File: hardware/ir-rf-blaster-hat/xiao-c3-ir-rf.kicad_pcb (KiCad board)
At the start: 2 copper layers, 21 x 50 mm, 18 parts, among them J1 XIAO_SOCKET_1x7, J2 XIAO_SOCKET_1x7, M1 CC1101_MODULE, Q1 SOT-23

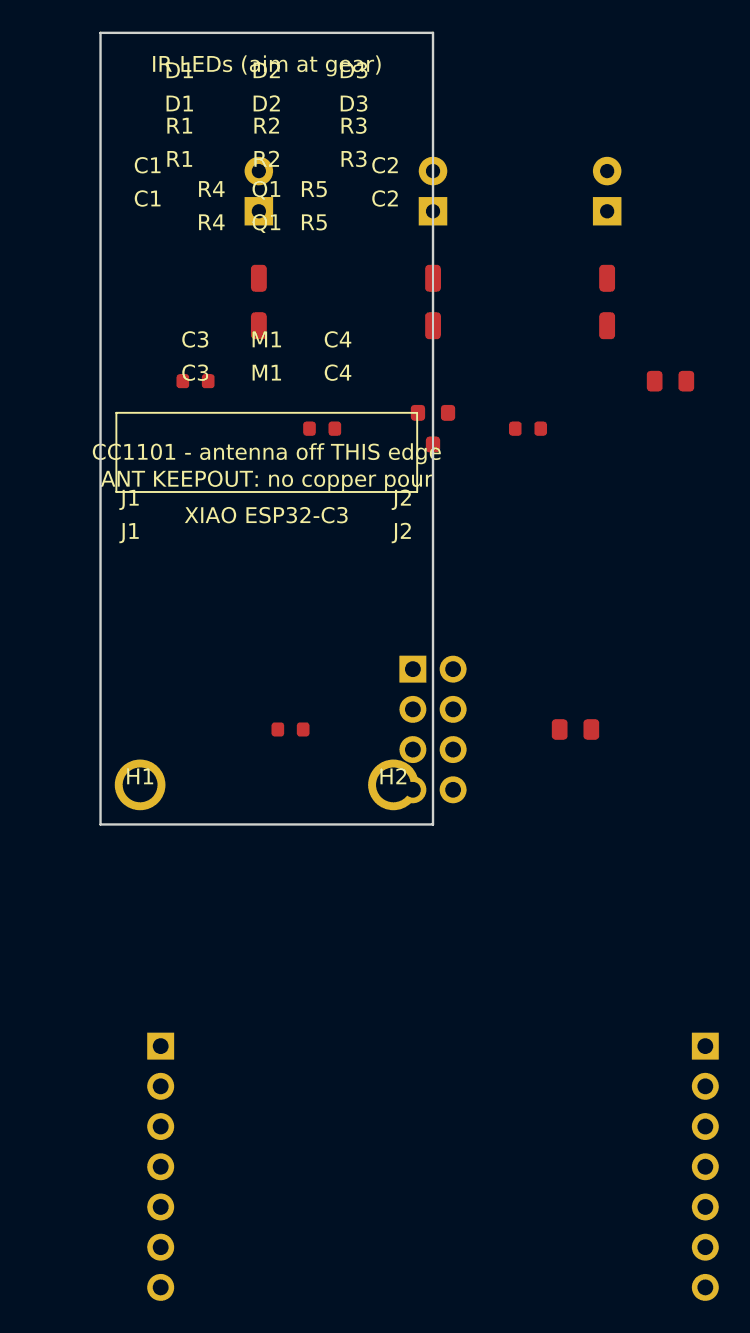
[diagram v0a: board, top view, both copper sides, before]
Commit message: feat(ir-rf-blaster): 4-layer, fully-routed, DRC-clean board (#1120)
* feat(ir-rf-blaster): 4-layer, fully-routed, DRC-clean board

Rebuild the XIAO IR+RF blaster hat as a 4-layer board, generated headlessly:
- Stackup F.Cu / In1.Cu GND plane / In2.Cu +5V plane / B.Cu. Real KiCad library
  footprints (was crude embedded geometry). GND/+5V stitched to planes via
  through-vias; +3V3 and logic signals routed on the outer layers.
- SPI fan-out uses a monotonic XIAO->CC1101 pin mapping so the traces don't cross.
- Validated with kicad-cli (KiCad 9): DRC 0 errors, 0 unconnected. Board 22x50mm.
- Ships generate_pcb.py (kiutils), fill_zones.py (pcbnew LoadBoard), the 8 footprints
  (offline-reproducible), the filled .kicad_pcb, a top render, and Gerbers/drill.

pcbnew scripting crashes under amd64 emulation on Apple Silicon (FootprintLoad), so
generation uses kiutils and zone-fill uses pcbnew.LoadBoard (which doesn't crash);
kicad-cli does DRC/export. Documented in the README.

Still GUI TODOs (flagged): swap the provisional XIAO socket for Seeed's official
footprint, and add the antenna copper keepout for the specific CC1101 module.

Co-Authored-By: Claude Opus 4.8 <noreply@anthropic.com>
Claude-Session: https://claude.ai/code/session_01NfkRErMrPyNuft1RbpzMet

* refactor(ir-rf-blaster): straighter, 45-degree, centered routing

- Straight diagonals where the line is clear (LED cathodes; SPI fan is already
  straight parallel), 45-degree chamfers on the rest (no 90-degree turns).
- Components centered east-west about the board centerline (x=11).
- Simplified the +3V3 tail to XIAO 3V3: straight drop + one 45-degree bend.
Still DRC-clean (0 errors, 0 unconnected). Re-exported Gerbers + render.

Co-Authored-By: Claude Opus 4.8 <noreply@anthropic.com>
Claude-Session: https://claude.ai/code/session_01NfkRErMrPyNuft1RbpzMet

* fix(ir-rf-blaster): center LEDs on board, fix off-board silk

Widen board to 23mm and center all components on the x=11.5 centerline so the
outer LEDs have 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
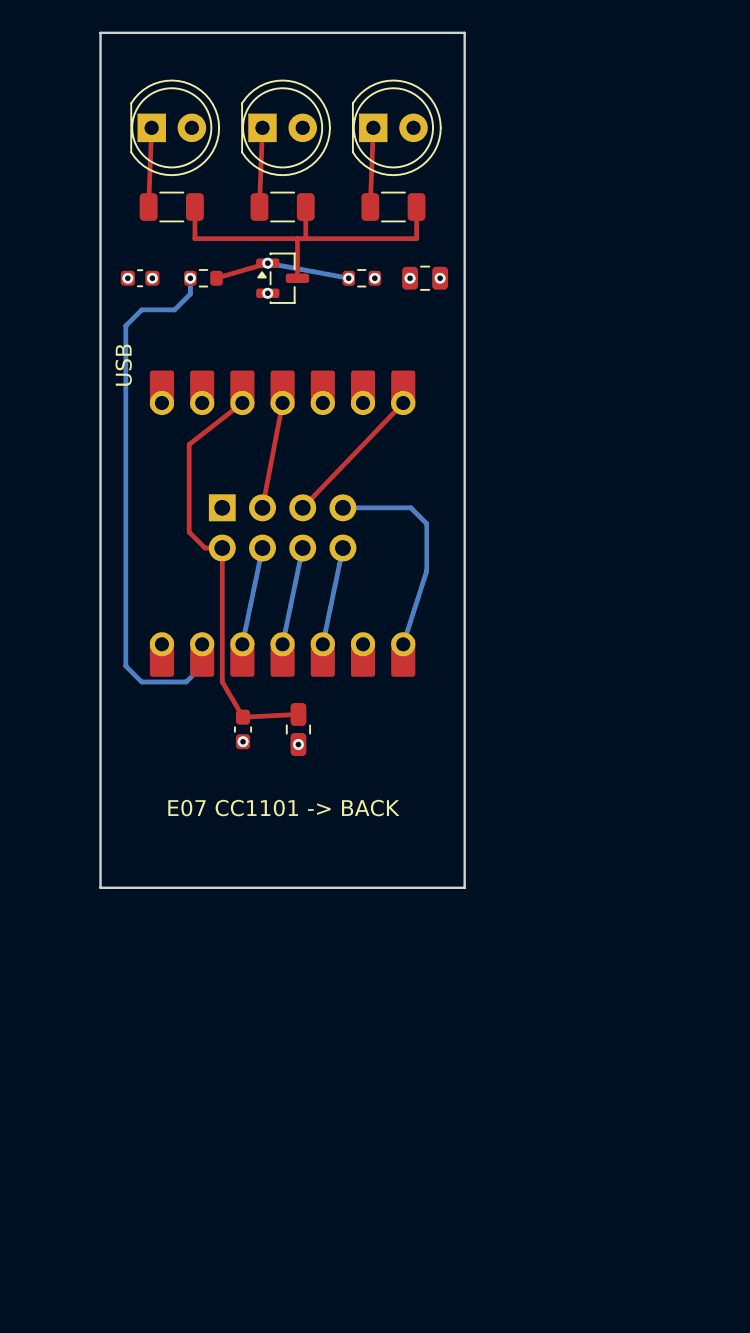
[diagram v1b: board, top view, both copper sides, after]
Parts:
- removed H1, H2: M2, hat:MountingHole_M2
- removed J1, J2: XIAO_SOCKET_1x7, hat:XIAO_SOCKET_1x7
- added A1: XIAO_ESP32C3, XIAO-ESP32-C3-DIP, F.Cu at (11.5, 31.0)
- C1, C3: value C_0603 -> 100nF; footprint hat:C_0603 -> C_0603_1608Metric
- C2: value C_0805 -> 22uF; footprint hat:C_0805 -> C_0805_2012Metric
- C4: value C_0805 -> 10uF; footprint hat:C_0805 -> C_0805_2012Metric
- D1, D2, D3: value LED_D5.0mm -> 940nm; footprint hat:LED_D5.0mm -> LED_D5.0mm
- M1: value CC1101_MODULE -> E07-M1101D; footprint hat:CC1101_MODULE -> PinSocket_2x04_P2.54mm_Vertical; moved to B.Cu
- Q1: value SOT-23 -> AO3400A; footprint hat:SOT-23 -> SOT-23
- R1, R2, R3: value R_1206 -> 15R; footprint hat:R_1206 -> R_1206_3216Metric
- R4: value R_0603 -> 100R; footprint hat:R_0603 -> R_0603_1608Metric
- R5: value R_0603 -> 10k; footprint hat:R_0603 -> R_0603_1608Metric
- moved C3 22.2 mm to (9.00, 44.0), turned to -90 degrees
- moved C4 22.1 mm to (12.5, 44.0), turned to -90 degrees
- moved M1 8.48 mm to (7.69, 30.0), turned to 90 degrees
- moved C2 5.15 mm to (20.5, 15.5)
- moved C1 4.53 mm to (2.50, 15.5)
- moved R5 4.24 mm to (16.5, 15.5)
- moved R3 3.54 mm to (18.5, 11.0)
- moved Q1 3.16 mm to (11.5, 15.5)
- moved R4 3.04 mm to (6.50, 15.5)
- moved R2 2.69 mm to (11.5, 11.0)
- moved R1 2.55 mm to (4.50, 11.0)
- moved D1 2.03 mm to (3.23, 6.00)
- moved D3 1.59 mm to (17.2, 6.00)
- moved D2 1.04 mm to (10.2, 6.00)
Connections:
- D1 pad 1: +5V -> LED1_K
- D1 pad 2: LED1_K -> +5V
- D2 pad 1: +5V -> LED2_K
- D2 pad 2: LED2_K -> +5V
- D3 pad 1: +5V -> LED3_K
- D3 pad 2: LED3_K -> +5V
- M1 pad 1: +3V3 -> GND
- M1 pad 2: GND -> +3V3
- M1 pad 3: CC_SCK -> CC_GDO0
- M1 pad 4: CC_MOSI -> CC_CSN
- M1 pad 5: CC_MISO -> CC_SCK
- M1 pad 6: CC_CSN -> CC_MOSI
- M1 pad 7: CC_GDO0 -> CC_MISO
- Q1 pad 1: IR_TX -> Q_GATE
- R4 pad 2: IR_TX -> Q_GATE
- R5 pad 1: IR_TX -> Q_GATE
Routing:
- net IR_TX: track 0.00 -> 34.4 mm, vias 0 -> 1
- net +3V3: track 0.00 -> 26.9 mm
- net Q_DRAIN: track 0.00 -> 22.5 mm
- net CC_MISO: track 0.00 -> 13.6 mm
- net CC_SCK: track 0.00 -> 9.17 mm
- net Q_GATE: track 0.00 -> 8.57 mm, vias 0 -> 2
- net CC_GDO0: track 0.00 -> 6.74 mm
- net CC_MOSI: track 0.00 -> 6.21 mm
- net CC_GDO2: track 0.00 -> 6.21 mm
- net CC_CSN: track 0.00 -> 6.21 mm
- net LED3_K: track 0.00 -> 5.00 mm
- net LED2_K: track 0.00 -> 5.00 mm
- net LED1_K: track 0.00 -> 5.00 mm
- net GND: vias 0 -> 6
- net +5V: vias 0 -> 2
- added copper zone on In2.Cu, net +5V
- added copper zone on In1.Cu, net GND
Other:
- board size 21 x 50 mm -> 23 x 54 mm
- copper layers 2 -> 4
- rule pad_to_mask_clearance: 0.0 -> 0
- board text added: "ANT v"
- board text added: "E07 CC1101 -> BACK"
- board text added: "USB"
- board text removed: "ANT KEEPOUT: no copper pour"
- board text removed: "C1"
- board text removed: "C2"
- board text removed: "C3"
- board text removed: "C4"
- board text removed: "CC1101 - antenna off THIS edge"
- board text removed: "D1"
- board text removed: "D2"
- board text removed: "D3"
- board text removed: "IR LEDs (aim at gear)"
- board text removed: "J1"
- board text removed: "J2"
- board text removed: "M1"
- board text removed: "Q1"
- board text removed: "R1"
- board text removed: "R2"
- board text removed: "R3"
- board text removed: "R4"
- board text removed: "R5"
- board text removed: "XIAO ESP32-C3"
